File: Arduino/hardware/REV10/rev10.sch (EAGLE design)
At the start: 46 parts, among them IC2 ATMEGA168-AU, Q1 32768Hz, U1 TC1185SMD, U2 ARDUINO

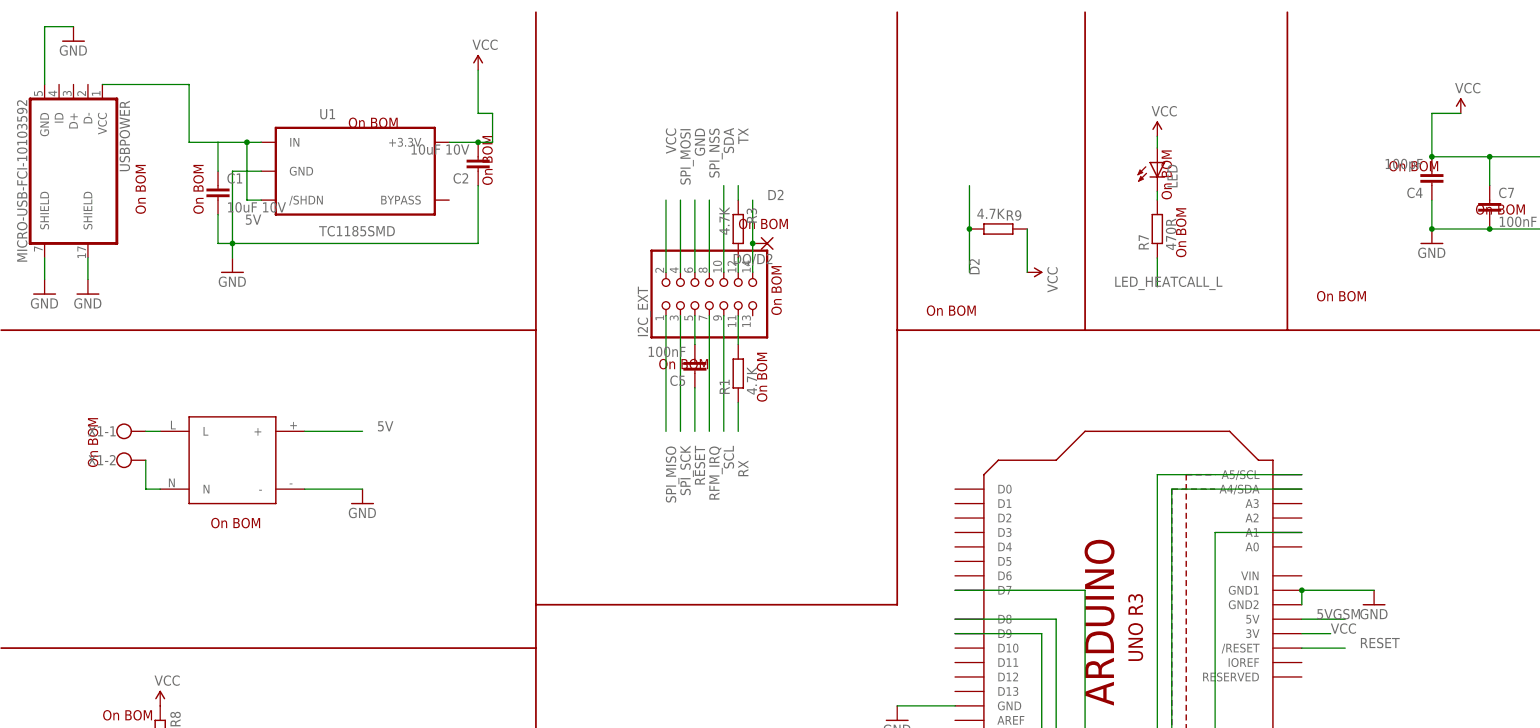
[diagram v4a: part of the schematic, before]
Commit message: rev10 and 11 updated as per deniz findings
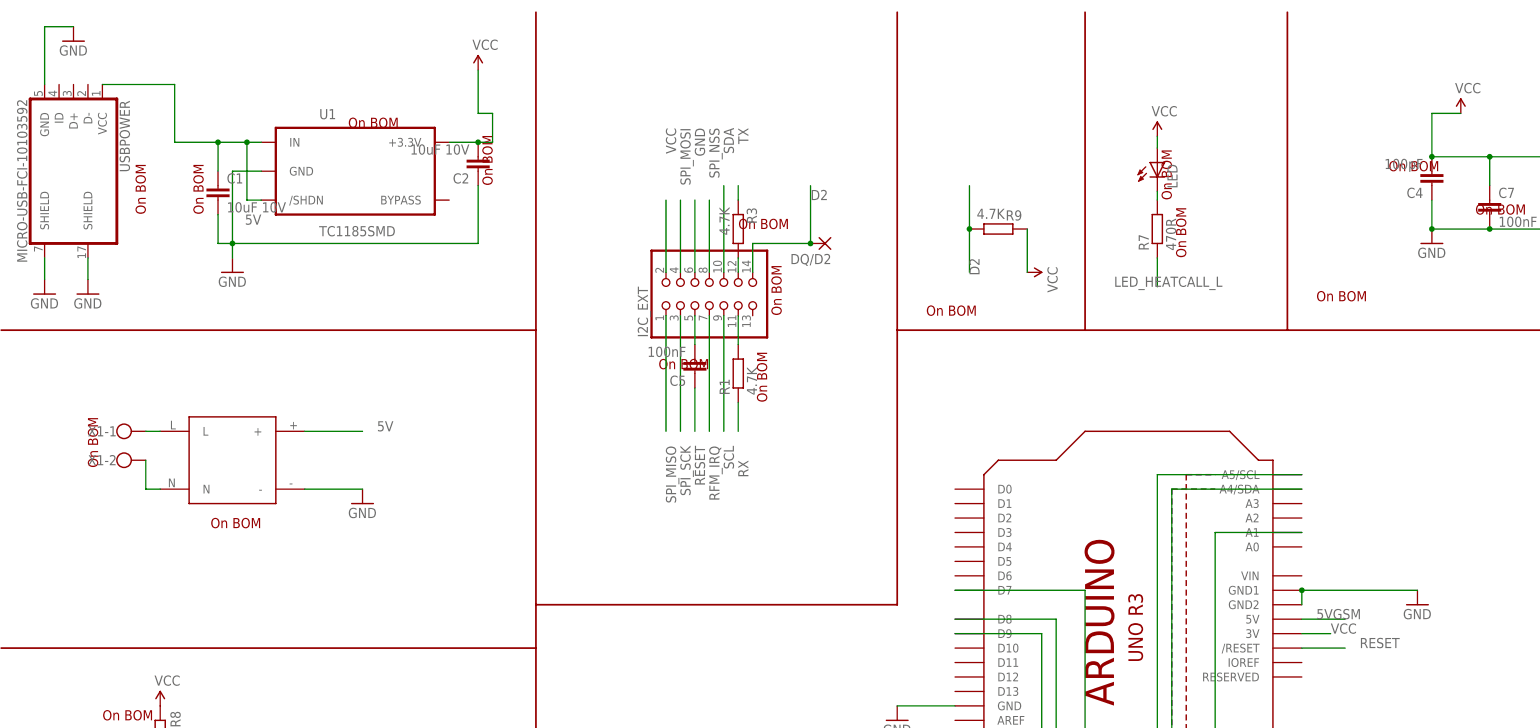
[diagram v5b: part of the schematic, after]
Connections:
- removed net 5V1: USBPOWER.VCC
- net 5V: now also USBPOWER.VCC
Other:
- moved on the sheet: DQ/D2
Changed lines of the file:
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@@
 <instance part="X1" gate="-1" x="20.32" y="190.5"/>
 <instance part="X1" gate="-2" x="20.32" y="185.42"/>
-<instance part="GND2" gate="1" x="241.3" y="160.02"/>
+<instance part="GND2" gate="1" x="248.92" y="160.02"/>
 <instance part="R1" gate="G$1" x="129.54" y="200.66" rot="R90"/>
 <instance part="R3" gate="G$1" x="129.54" y="226.06" rot="R270"/>
@@
 <instance part="R5" gate="G$1" x="200.66" y="73.66" rot="R180"/>
 <instance part="R17" gate="G$1" x="182.88" y="101.6" rot="R270"/>
-<instance part="DQ/D2" gate="1" x="134.62" y="223.52" rot="R180"/>
+<instance part="DQ/D2" gate="1" x="144.78" y="223.52" rot="R180"/>
 </instances>
 <busses>
@@
 <pinref part="U2" gate="G$1" pin="GND1"/>
 <pinref part="GND2" gate="1" pin="GND"/>
-<wire x1="241.3" y1="162.56" x2="228.6" y2="162.56" width="0.1524" layer="91"/>
+<wire x1="248.92" y1="162.56" x2="228.6" y2="162.56" width="0.1524" layer="91"/>
 <pinref part="U2" gate="G$1" pin="GND2"/>
 <wire x1="228.6" y1="162.56" x2="228.6" y2="160.02" width="0.1524" layer="91"/>
@@
 <pinref part="U1" gate="G$1" pin="/SHDN"/>
 <label x="45.72" y="228.6" size="1.778" layer="95" rot="R180"/>
+<wire x1="17.78" y1="251.46" x2="30.48" y2="251.46" width="0.1524" layer="91"/>
+<wire x1="30.48" y1="251.46" x2="30.48" y2="241.3" width="0.1524" layer="91"/>
+<wire x1="30.48" y1="241.3" x2="38.1" y2="241.3" width="0.1524" layer="91"/>
+<pinref part="USBPOWER" gate="G$1" pin="VCC"/>
+<junction x="38.1" y="241.3"/>
 </segment>
 <segment>
@@
 <net name="D2" class="0">
 <segment>
-<wire x1="132.08" y1="231.14" x2="132.08" y2="223.52" width="0.1524" layer="91"/>
-<label x="134.62" y="231.14" size="1.778" layer="95"/>
+<wire x1="142.24" y1="233.68" x2="142.24" y2="223.52" width="0.1524" layer="91"/>
+<label x="142.24" y="231.14" size="1.778" layer="95"/>
 <pinref part="I2C_EXT" gate="A" pin="14"/>
 <pinref part="DQ/D2" gate="1" pin="P"/>
+<wire x1="142.24" y1="223.52" x2="132.08" y2="223.52" width="0.1524" layer="91"/>
 <wire x1="132.08" y1="223.52" x2="132.08" y2="218.44" width="0.1524" layer="91"/>
-<junction x="132.08" y="223.52"/>
+<junction x="142.24" y="223.52"/>
 </segment>
 <segment>
@@
 </segment>
 </net>
-<net name="5V1" class="1">
-<segment>
-<wire x1="17.78" y1="251.46" x2="33.02" y2="251.46" width="0.1524" layer="91"/>
-<wire x1="33.02" y1="251.46" x2="33.02" y2="241.3" width="0.1524" layer="91"/>
-<wire x1="33.02" y1="241.3" x2="38.1" y2="241.3" width="0.1524" layer="91"/>
-<pinref part="USBPOWER" gate="G$1" pin="VCC"/>
-</segment>
-</net>

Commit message: rev10 reworked as per marks instruction. Almost ready for eyeball
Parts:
- I2C_EXT: device pinhead:PINHD-2X7/90 -> pinhead:PINHD-2X7
- JP2: device pinhead:PINHD-2X3/90 -> pinhead:PINHD-2X3
- renumbered DQ/D2 to DQ
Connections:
- removed net N$24: REL1.S, X3-1.KL
- new net N$21: REL1.C, X3-1.KL
- net N$22: now also REL1.S; no longer REL1.C
- net N$4: now also X1-1.KL; no longer X1-2.KL
- net N$8: now also X1-2.KL; no longer X1-1.KL
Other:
- moved on the sheet: X1-1, X1-2, X3-1, X3-2
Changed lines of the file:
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@@
 <part name="R3" library="resistor" deviceset="R-EU_" device="R0603" value="4.7K"/>
 <part name="C5" library="resistor" deviceset="C-EU" device="C0603" value="100nF"/>
-<part name="I2C_EXT" library="pinhead" deviceset="PINHD-2X7" device="/90"/>
+<part name="I2C_EXT" library="pinhead" deviceset="PINHD-2X7" device=""/>
 <part name="IC2" library="Arduino-AVR" deviceset="ATMEGA168" device="-AU"/>
 <part name="USBPOWER" library="micro-usb-fci-10103592" deviceset="MICRO-USB-FCI-10103592" device=""/>
@@
 <part name="R14" library="resistor" deviceset="R-EU_" device="R0603" value="10K"/>
 <part name="GND10" library="SparkFun-Aesthetics" deviceset="GND" device=""/>
-<part name="JP2" library="pinhead" deviceset="PINHD-2X3" device="/90"/>
+<part name="JP2" library="pinhead" deviceset="PINHD-2X3" device=""/>
 <part name="PFET" library="transistor-small-signal" deviceset="BSS84" device=""/>
 <part name="R15" library="resistor" deviceset="R-EU_" device="R0603" value="4.7K"/>
@@
 <part name="R5" library="resistor" deviceset="R-EU_" device="R0603" value="4.7K"/>
 <part name="R17" library="resistor" deviceset="R-EU_" device="R0603" value="4.7K"/>
-<part name="DQ/D2" library="wirepad" deviceset="2,15/1,0" device=""/>
+<part name="DQ" library="wirepad" deviceset="2,15/1,0" device=""/>
 </parts>
 <sheets>
@@
 <instance part="U2" gate="G$1" x="223.52" y="127" rot="R90"/>
 <instance part="GND1" gate="1" x="63.5" y="177.8"/>
-<instance part="X1" gate="-1" x="20.32" y="190.5"/>
-<instance part="X1" gate="-2" x="20.32" y="185.42"/>
+<instance part="X1" gate="-1" x="20.32" y="180.34"/>
+<instance part="X1" gate="-2" x="20.32" y="190.5"/>
 <instance part="GND2" gate="1" x="248.92" y="160.02"/>
 <instance part="R1" gate="G$1" x="129.54" y="200.66" rot="R90"/>
@@
 </instance>
 <instance part="REL1" gate="G$1" x="358.14" y="93.98" rot="R270"/>
-<instance part="X3" gate="-1" x="342.9" y="96.52"/>
-<instance part="X3" gate="-2" x="342.9" y="91.44"/>
+<instance part="X3" gate="-1" x="340.36" y="91.44"/>
+<instance part="X3" gate="-2" x="340.36" y="96.52"/>
 <instance part="R16" gate="G$1" x="185.42" y="119.38" rot="R270"/>
 <instance part="R5" gate="G$1" x="200.66" y="73.66" rot="R180"/>
 <instance part="R17" gate="G$1" x="182.88" y="101.6" rot="R270"/>
-<instance part="DQ/D2" gate="1" x="144.78" y="223.52" rot="R180"/>
+<instance part="DQ" gate="1" x="144.78" y="223.52" rot="R180"/>
 </instances>
 <busses>
@@
 <net name="N$4" class="0">
 <segment>
-<pinref part="X1" gate="-2" pin="KL"/>
-<wire x1="25.4" y1="185.42" x2="25.4" y2="180.34" width="0.1524" layer="91"/>
 <wire x1="25.4" y1="180.34" x2="27.94" y2="180.34" width="0.1524" layer="91"/>
 <pinref part="PSU" gate="G$1" pin="N"/>
-</segment>
-</net>
-<net name="N$8" class="0">
-<segment>
 <pinref part="X1" gate="-1" pin="KL"/>
-<wire x1="25.4" y1="190.5" x2="27.94" y2="190.5" width="0.1524" layer="91"/>
-<pinref part="PSU" gate="G$1" pin="L"/>
 </segment>
 </net>
@@
 <label x="142.24" y="231.14" size="1.778" layer="95"/>
 <pinref part="I2C_EXT" gate="A" pin="14"/>
-<pinref part="DQ/D2" gate="1" pin="P"/>
+<pinref part="DQ" gate="1" pin="P"/>
 <wire x1="142.24" y1="223.52" x2="132.08" y2="223.52" width="0.1524" layer="91"/>
 <wire x1="132.08" y1="223.52" x2="132.08" y2="218.44" width="0.1524" layer="91"/>
@@
 </segment>
 </net>
-<net name="N$22" class="0">
-<segment>
-<pinref part="REL1" gate="G$1" pin="C"/>
-<pinref part="X3" gate="-2" pin="KL"/>
-</segment>
-</net>
-<net name="N$24" class="0">
-<segment>
-<pinref part="REL1" gate="G$1" pin="S"/>
-<pinref part="X3" gate="-1" pin="KL"/>
-</segment>
-</net>
 <net name="N$30" class="0">
 <segment>
@@
 </segment>
 </net>
+<net name="N$8" class="0">
+<segment>
+<pinref part="PSU" gate="G$1" pin="L"/>
+<pinref part="X1" gate="-2" pin="KL"/>
+<wire x1="25.4" y1="190.5" x2="27.94" y2="190.5" width="0.1524" layer="91"/>
+</segment>
+</net>
+<net name="N$21" class="0">
+<segment>
+<pinref part="REL1" gate="G$1" pin="C"/>
+<pinref part="X3" gate="-1" pin="KL"/>
+<wire x1="345.44" y1="91.44" x2="347.98" y2="91.44" width="0.1524" layer="91"/>
+</segment>
+</net>
+<net name="N$22" class="0">
+<segment>
+<pinref part="REL1" gate="G$1" pin="S"/>
+<pinref part="X3" gate="-2" pin="KL"/>
+<wire x1="345.44" y1="96.52" x2="347.98" y2="96.52" width="0.1524" layer="91"/>
+</segment>
+</net>

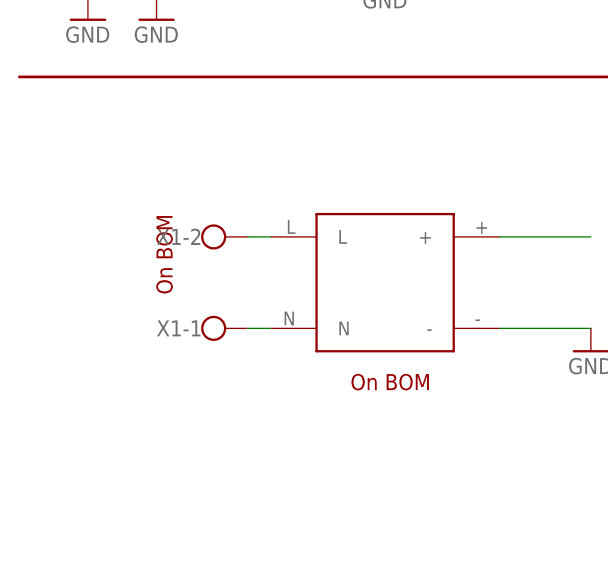
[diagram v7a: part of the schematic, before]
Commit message: more corrections to rev10
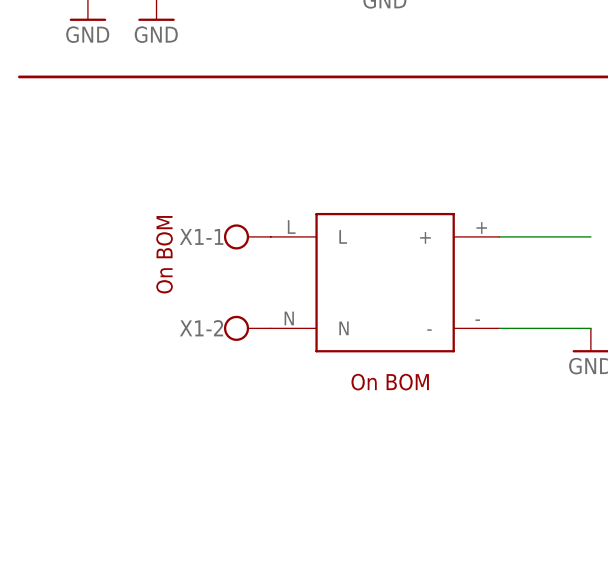
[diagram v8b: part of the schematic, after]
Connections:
- net N$4: now also X1-2.KL; no longer X1-1.KL
- net N$8: now also X1-1.KL; no longer X1-2.KL
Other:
- moved on the sheet: X1-1, X1-2
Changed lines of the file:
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@@
 <instance part="U2" gate="G$1" x="223.52" y="127" rot="R90"/>
 <instance part="GND1" gate="1" x="63.5" y="177.8"/>
-<instance part="X1" gate="-1" x="20.32" y="180.34"/>
-<instance part="X1" gate="-2" x="20.32" y="190.5"/>
+<instance part="X1" gate="-1" x="22.86" y="190.5"/>
+<instance part="X1" gate="-2" x="22.86" y="180.34"/>
 <instance part="GND2" gate="1" x="248.92" y="160.02"/>
 <instance part="R1" gate="G$1" x="129.54" y="200.66" rot="R90"/>
@@
 </segment>
 </net>
-<net name="N$4" class="0">
-<segment>
-<wire x1="25.4" y1="180.34" x2="27.94" y2="180.34" width="0.1524" layer="91"/>
-<pinref part="PSU" gate="G$1" pin="N"/>
-<pinref part="X1" gate="-1" pin="KL"/>
-</segment>
-</net>
 <net name="N$15" class="0">
 <segment>
@@
 </segment>
 </net>
-<net name="N$8" class="0">
-<segment>
-<pinref part="PSU" gate="G$1" pin="L"/>
-<pinref part="X1" gate="-2" pin="KL"/>
-<wire x1="25.4" y1="190.5" x2="27.94" y2="190.5" width="0.1524" layer="91"/>
-</segment>
-</net>
 <net name="N$21" class="0">
 <segment>
@@
 </segment>
 </net>
+<net name="N$4" class="0">
+<segment>
+<pinref part="PSU" gate="G$1" pin="N"/>
+<pinref part="X1" gate="-2" pin="KL"/>
+</segment>
+</net>
+<net name="N$8" class="0">
+<segment>
+<pinref part="PSU" gate="G$1" pin="L"/>
+<pinref part="X1" gate="-1" pin="KL"/>
+</segment>
+</net>
